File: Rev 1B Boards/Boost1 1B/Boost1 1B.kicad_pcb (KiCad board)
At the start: 4 copper layers, 46 x 71.2 mm, 43 parts, among them J18 Banana 2P, J19 Banana 2P, J20 Banana 2P, Q1 BSC059N04LS6, Q2 BSC059N04LS6, Q3 BSC059N04LS6, U1 LM74700, U2 LM5123-Q1

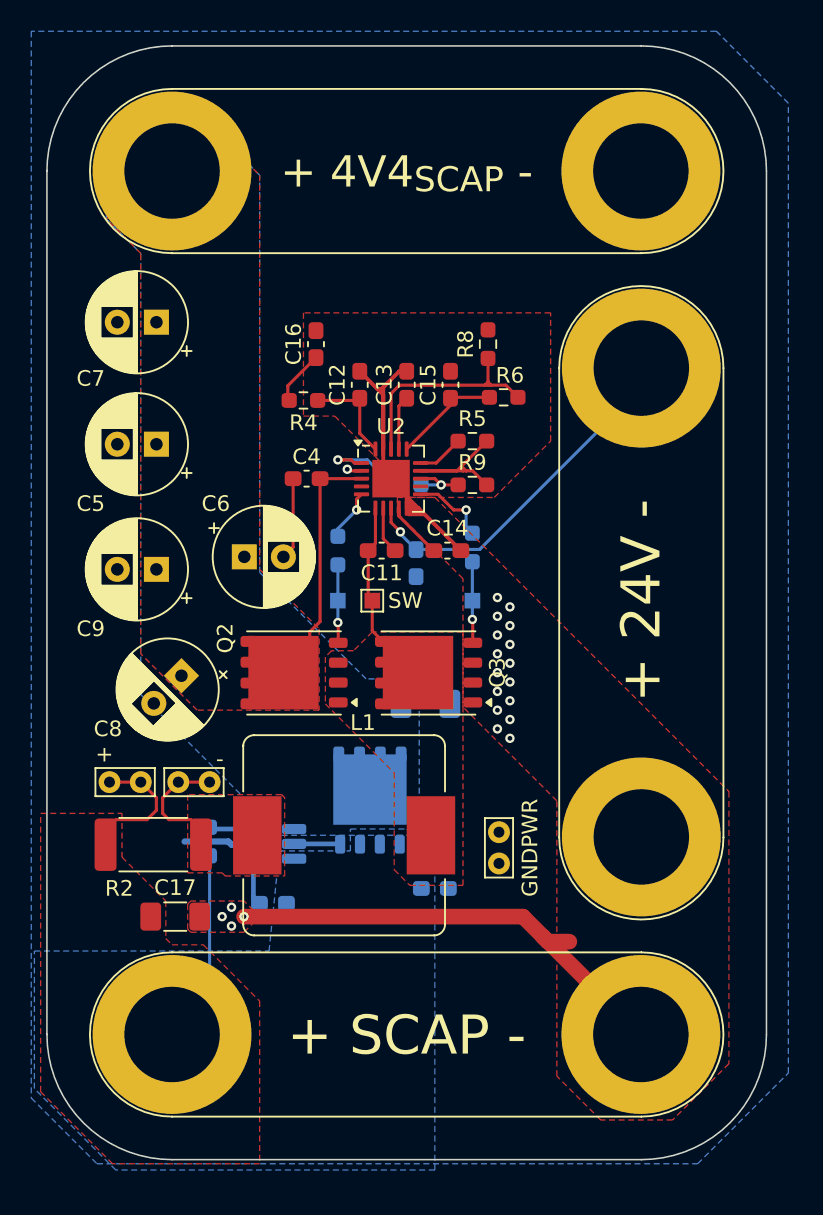
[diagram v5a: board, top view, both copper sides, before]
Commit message: Replace most banana jacks with XT connectors
+ update library
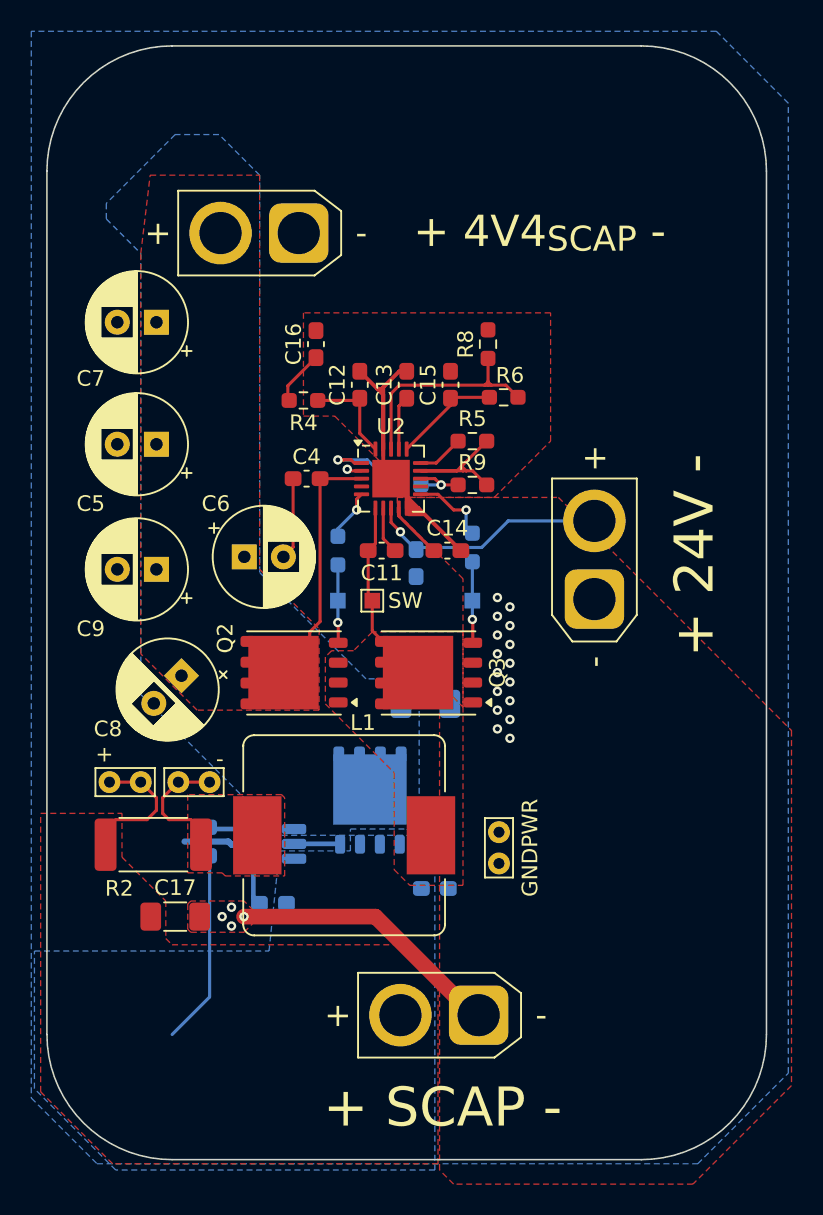
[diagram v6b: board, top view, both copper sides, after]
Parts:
- removed J18, J19, J20: Banana 2P, Connector:Banana_Jack_2Pin
- added J14: XT30_F, Connector_AMASS:AMASS_XT30U-F_1x02_P5.0mm_Vertical, F.Cu at (130.8, 125.7)
- added J15: XT30_F, Connector_AMASS:AMASS_XT30U-F_1x02_P5.0mm_Vertical, F.Cu at (119.3, 75.7)
- added J16: XT30_F, Connector_AMASS:AMASS_XT30U-F_1x02_P5.0mm_Vertical, F.Cu at (138.2, 99.1)
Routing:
- net GNDPWR: track 73.1 -> 60.4 mm
- net +24V: track 23.3 -> 15.5 mm
